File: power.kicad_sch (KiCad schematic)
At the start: 9 parts, among them U5 TPSM863257RDX

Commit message: revised a little bit
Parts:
- C24: DK (none) -> 399-C0805C106K8PAC7800CT-ND
- R10: DK (none) -> 541-19.1KLCT-ND
- R11: DK (none) -> 311-10KJRCT-ND; PARTNO CRCW040210K0FKED -> RC0402JR-0710KL
- R13: DK (none) -> 311-30.0KHRCT-ND
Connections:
- net PEN: now reaches C11.1, R10.2, R11.1, U5.6 (EN)
- net PGOOD: now reaches U5.5 (PG)
- no-connect marks 2 -> 1
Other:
- moved on the sheet: C10, C23, C24, R10, R11, R12, R13

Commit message: ready to go
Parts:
- removed C11: 10nF, Capacitor_SMD:C_0402_1005Metric, symbol Device:C
- removed R10: 19.1k, Resistor_SMD:R_0402_1005Metric, symbol Device:R_US
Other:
- moved on the sheet: C23, C24, R11

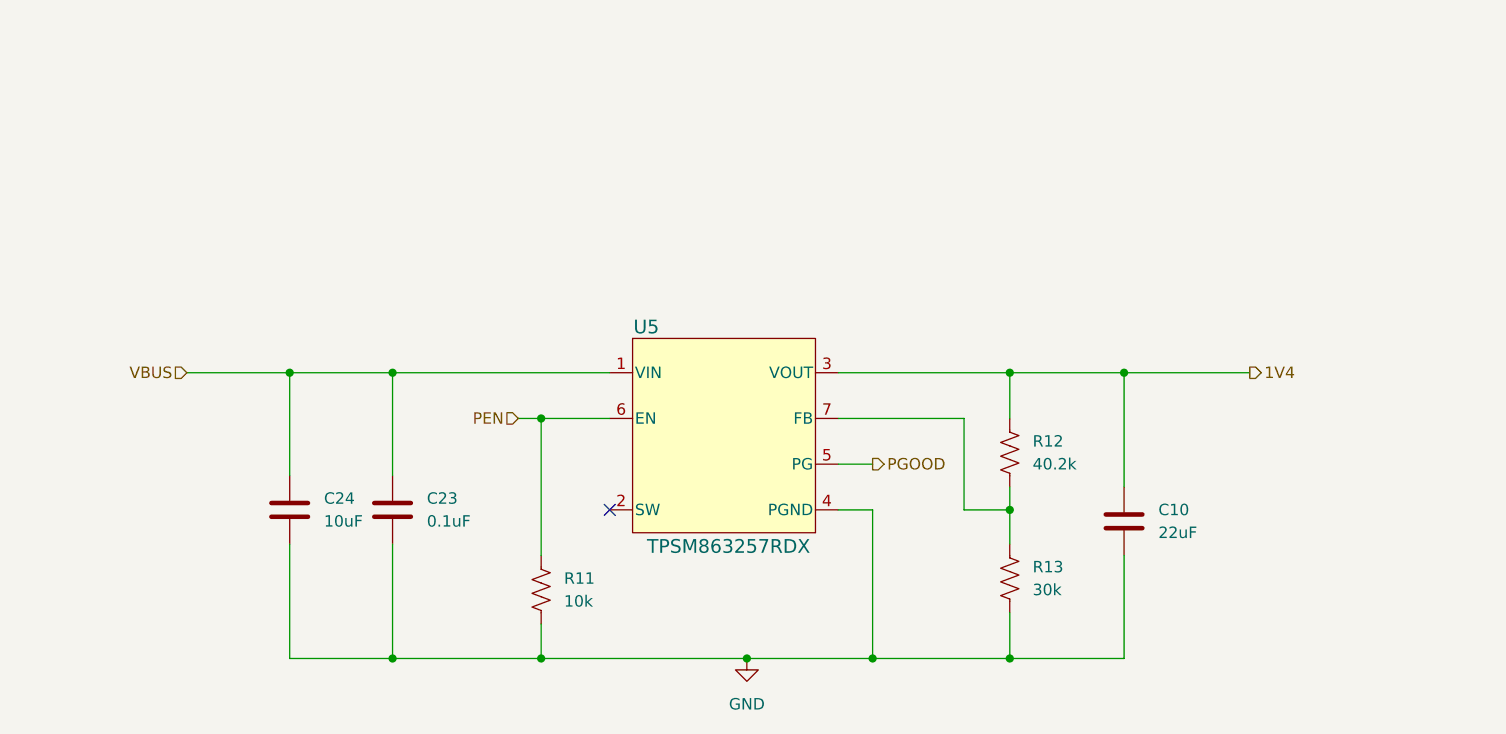
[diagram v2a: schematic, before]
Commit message: other buck converter
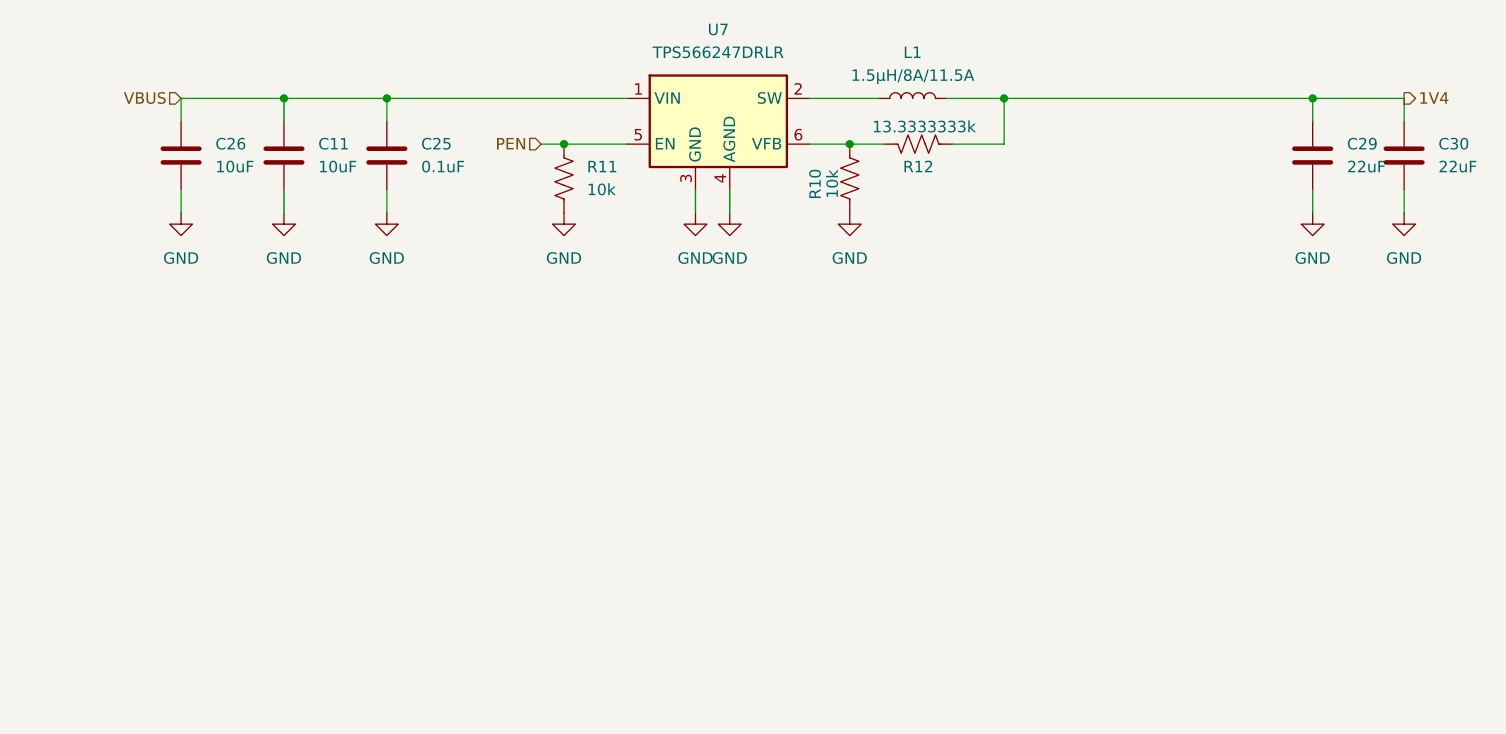
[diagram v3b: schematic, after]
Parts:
- removed C10: 22uF, Capacitor_SMD:C_0603_1608Metric, symbol Device:C
- removed C23: 0.1uF, Capacitor_SMD:C_0402_1005Metric, symbol Device:C
- removed C24: 10uF, Capacitor_SMD:C_0805_2012Metric, symbol Device:C
- removed R13: 30k, Resistor_SMD:R_0603_1608Metric, symbol Device:R_US
- removed U5: TPSM863257RDX, bitaxe:TPSM863257RDX, symbol bitaxe:TPSM863257RDX
- added C11, C26: 10uF, Capacitor_SMD:C_0805_2012Metric, symbol Device:C
- added C25: 0.1uF, Capacitor_SMD:C_0402_1005Metric, symbol Device:C
- added C29, C30: 22uF, Capacitor_SMD:C_0805_2012Metric, symbol Device:C
- added L1: 1.5µH/8A/11.5A, Inductor_SMD:L_Cenker_CKCS8040, symbol Device:L
- added R10: 10k, Resistor_SMD:R_0402_1005Metric, symbol Device:R_US
- added U7: TPS566247DRLR, myfootprints:SOT-563, symbol mylib7:TPS56624x
- R12: value 40.2k -> 13.3333333k; footprint Resistor_SMD:R_0603_1608Metric -> Resistor_SMD:R_0402_1005Metric
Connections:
- net 1V4: now also R12.2, C29.1, C30.1, L1.2; no longer R12.1
- net GND: now also C11.2, C25.2, C26.2, C29.2, C30.2, R10.1, U7.3 (GND), U7.4 (AGND)
- net PEN: now also U7.5 (EN)
- net VBUS: now also C11.1, C25.1, C26.1, U7.1 (VIN)
- new net: L1.1, U7.2 (SW)
- new net: R10.2, R12.1, U7.6 (VFB)
- no-connect marks 1 -> 0
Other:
- moved on the sheet: R11, R12

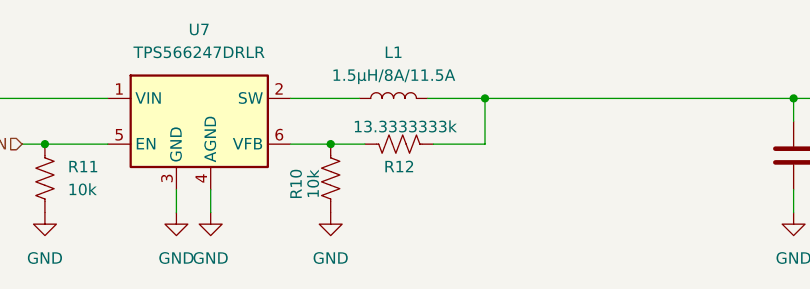
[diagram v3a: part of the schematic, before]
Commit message: fixed 2 resistor order numbers
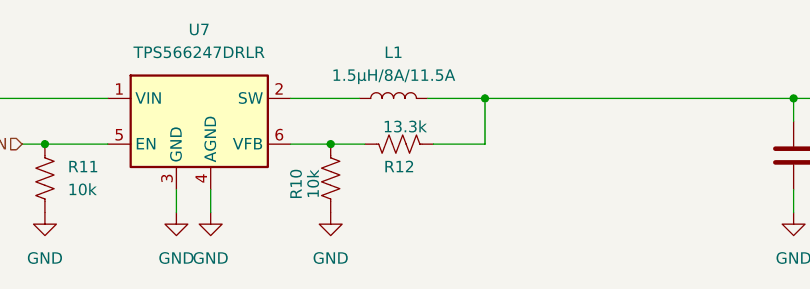
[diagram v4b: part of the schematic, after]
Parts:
- R10: DK 311-40.2KHRTR-ND -> 311-10KJRCT-ND
- R12: value 13.3333333k -> 13.3k; DK 311-40.2KHRTR-ND -> P13.3KLCT-ND
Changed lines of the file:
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@@
 			)
 		)
-		(property "Value" "13.3333333k"
+		(property "Value" "13.3k"
 			(at 160.655 73.025 90)
 			(effects
@@
 			)
 		)
-		(property "DK" "311-40.2KHRTR-ND"
+		(property "DK" "P13.3KLCT-ND"
 			(at 160.02 74.93 0)
 			(effects
@@
 			)
 		)
-		(property "DK" "311-40.2KHRTR-ND"
+		(property "DK" "311-10KJRCT-ND"
 			(at 152.4 78.74 0)
 			(effects

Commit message: fixed 22uF digi order number, added 2pin header for fan
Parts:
- C29, C30: DK 490-7611-1-ND -> 1276-6687-1-ND
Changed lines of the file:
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@@
 			)
 		)
-		(property "Datasheet" "https://www.ti.com/lit/gpn/tps562202"
+		(property "Datasheet" ""
 			(at 137.795 72.39 0)
 			(effects
@@
 			)
 		)
-		(property "Description" "2A Synchronous Step-Down Voltage Regulator 580kHz, adjustable output voltage, 4.5-17V Input Voltage, 0.804V-7V Output Voltage, SOT-563"
+		(property "Description" ""
 			(at 137.795 72.39 0)
 			(effects
@@
 			)
 		)
-		(property "DK" "490-7611-1-ND"
+		(property "DK" "1276-6687-1-ND"
 			(at 213.995 76.2 0)
 			(effects
@@
 			)
 		)
-		(property "DK" "490-7611-1-ND"
+		(property "DK" "1276-6687-1-ND"
 			(at 203.835 76.2 0)
 			(effects
